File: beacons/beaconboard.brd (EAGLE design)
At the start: 101.6 x 76.2 mm, 33 parts, among them IC1 7805TV, Q1 2N3904

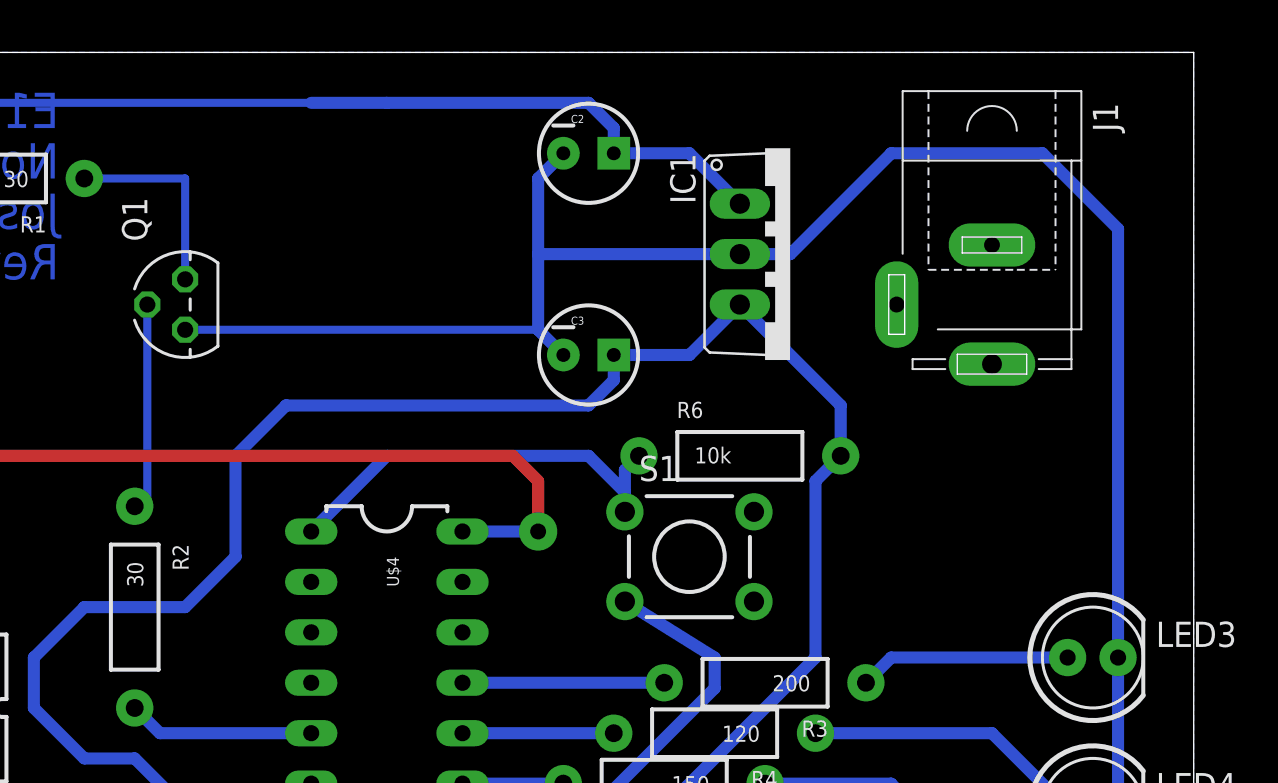
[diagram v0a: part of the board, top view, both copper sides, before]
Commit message: added DC jack; fixed NPN base resistor val
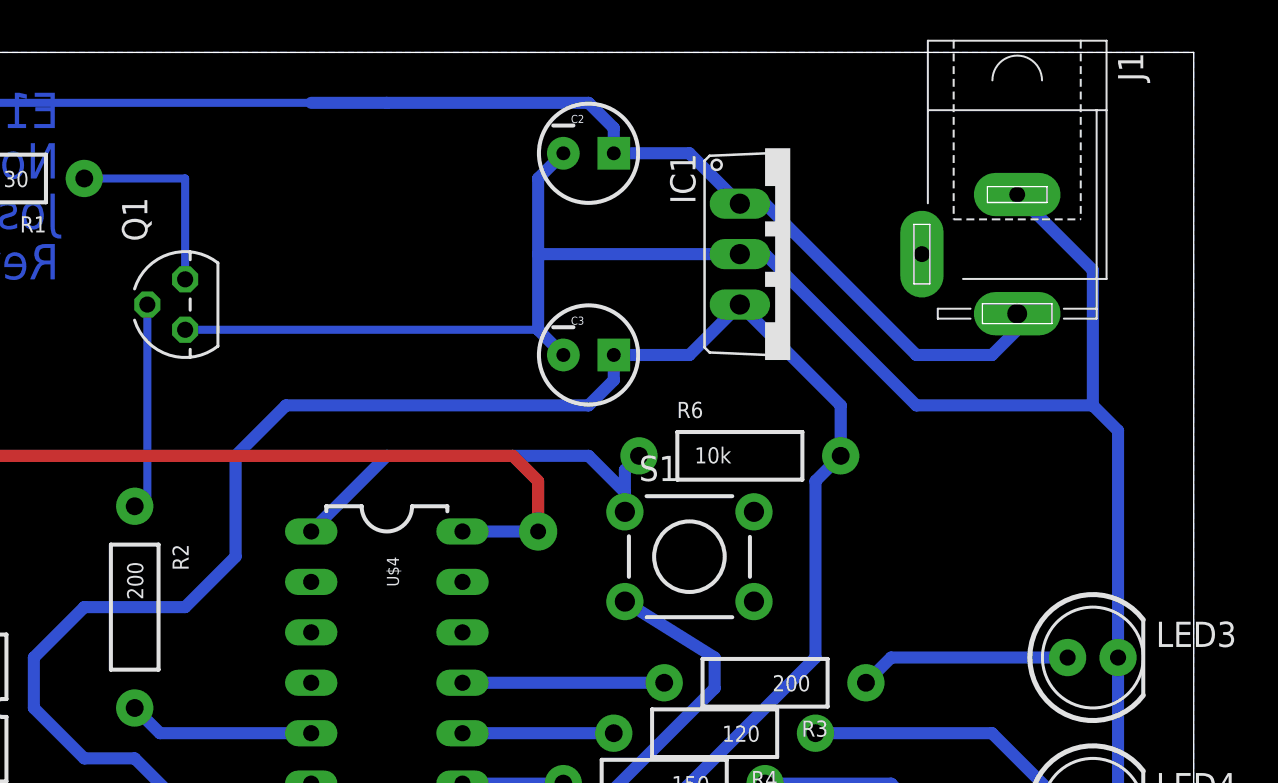
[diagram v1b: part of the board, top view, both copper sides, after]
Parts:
- R2: value 30 -> 200
- moved J1 2.84 mm to (92.7, 66.0)
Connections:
- net GND: now also J1.1
- net VDD: now also J1.3
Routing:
- net VDD: track 87.9 -> 106.4 mm
- net GND: track 409.8 -> 411.9 mm
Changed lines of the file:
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@@
 <element name="U$4" library="hmcfabstudio" package="DIL28-3" value="ATMEGA328" x="60.96" y="35.56" rot="R270"/>
 <element name="Q1" library="transistor-small-signal" package="TO92D" value="2N3904" x="50.8" y="63.5" rot="R90"/>
-<element name="J1" library="con-jack" package="SPC4078" value="" x="91.44" y="63.5" rot="R270">
-<attribute name="OC_NEWARK" value="unknown" x="91.44" y="63.5" size="1.778" layer="27" rot="R270" display="off"/>
-<attribute name="MPN" value="" x="91.44" y="63.5" size="1.778" layer="27" rot="R270" display="off"/>
-<attribute name="MF" value="" x="91.44" y="63.5" size="1.778" layer="27" rot="R270" display="off"/>
-<attribute name="OC_FARNELL" value="unknown" x="91.44" y="63.5" size="1.778" layer="27" rot="R270" display="off"/>
+<element name="J1" library="con-jack" package="SPC4078" value="" x="92.71" y="66.04" rot="R270">
+<attribute name="OC_NEWARK" value="unknown" x="92.71" y="66.04" size="1.778" layer="27" rot="R270" display="off"/>
+<attribute name="MPN" value="" x="92.71" y="66.04" size="1.778" layer="27" rot="R270" display="off"/>
+<attribute name="MF" value="" x="92.71" y="66.04" size="1.778" layer="27" rot="R270" display="off"/>
+<attribute name="OC_FARNELL" value="unknown" x="92.71" y="66.04" size="1.778" layer="27" rot="R270" display="off"/>
 </element>
 <element name="IC1" library="linear" package="TO220V" value="7805TV" x="81.28" y="66.04" rot="R270"/>
@@
 <element name="LED2" library="led" package="CP41B" value="" x="38.1" y="33.02" rot="R90"/>
 <element name="R1" library="SparkFun-Resistors" package="AXIAL-0.4" value="30" x="40.64" y="69.85" rot="R180"/>
-<element name="R2" library="SparkFun-Resistors" package="AXIAL-0.4" value="30" x="48.26" y="48.26" rot="R270"/>
+<element name="R2" library="SparkFun-Resistors" package="AXIAL-0.4" value="200" x="48.26" y="48.26" rot="R270"/>
 <element name="R3" library="SparkFun-Resistors" package="AXIAL-0.4" value="200" x="80.01" y="44.45" rot="R180"/>
 <element name="R4" library="SparkFun-Resistors" package="AXIAL-0.4" value="120" x="77.47" y="41.91" rot="R180"/>
@@
 <wire x1="27.94" y1="7.62" x2="31.75" y2="3.81" width="0.6096" layer="16"/>
 <wire x1="46.99" y1="3.81" x2="31.75" y2="3.81" width="0.6096" layer="16"/>
-<wire x1="86.36" y1="71.12" x2="81.28" y2="66.04" width="0.6096" layer="16"/>
-<wire x1="81.28" y1="66.04" x2="78.74" y2="66.04" width="0.6096" layer="16"/>
-<wire x1="86.36" y1="71.12" x2="93.98" y2="71.12" width="0.6096" layer="16"/>
-<wire x1="93.98" y1="71.12" x2="97.79" y2="67.31" width="0.6096" layer="16"/>
-<wire x1="97.79" y1="67.31" x2="97.79" y2="45.72" width="0.6096" layer="16"/>
+<wire x1="87.63" y1="58.42" x2="80.01" y2="66.04" width="0.6096" layer="16"/>
+<wire x1="80.01" y1="66.04" x2="78.74" y2="66.04" width="0.6096" layer="16"/>
+<wire x1="87.63" y1="58.42" x2="96.52" y2="58.42" width="0.6096" layer="16"/>
+<wire x1="96.52" y1="58.42" x2="97.79" y2="57.15" width="0.6096" layer="16"/>
+<wire x1="97.79" y1="57.15" x2="97.79" y2="45.72" width="0.6096" layer="16"/>
 <wire x1="40.64" y1="25.4" x2="40.64" y2="27.94" width="0.6096" layer="16"/>
 <wire x1="40.64" y1="27.94" x2="48.26" y2="35.56" width="0.6096" layer="16"/>
@@
 <wire x1="50.8" y1="62.23" x2="68.58" y2="62.23" width="0.4064" layer="16"/>
 <wire x1="27.94" y1="10.16" x2="27.94" y2="25.4" width="0.4064" layer="16"/>
-<wire x1="5.08" y1="36.83" x2="5.08" y2="38.1" width="0" layer="19" extent="16-16"/>
+<contactref element="J1" pad="1"/>
+<wire x1="96.52" y1="58.42" x2="96.52" y2="65.23" width="0.6096" layer="16"/>
+<wire x1="96.52" y1="65.23" x2="92.71" y2="69.04" width="0.6096" layer="16"/>
 </signal>
 <signal name="VDD">
@@
 <wire x1="40.64" y1="45.72" x2="40.64" y2="73.66" width="0.4064" layer="16"/>
 <wire x1="40.64" y1="73.66" x2="60.96" y2="73.66" width="0.4064" layer="16"/>
+<contactref element="J1" pad="3"/>
+<wire x1="92.71" y1="63.04" x2="92.71" y2="62.23" width="0.6096" layer="16"/>
+<wire x1="92.71" y1="62.23" x2="91.44" y2="60.96" width="0.6096" layer="16"/>
+<wire x1="91.44" y1="60.96" x2="87.63" y2="60.96" width="0.6096" layer="16"/>
+<wire x1="87.63" y1="60.96" x2="80.01" y2="68.58" width="0.6096" layer="16"/>
+<wire x1="80.01" y1="68.58" x2="78.74" y2="68.58" width="0.6096" layer="16"/>
 <wire x1="40.64" y1="35.56" x2="40.64" y2="40.64" width="0" layer="19" extent="1-1"/>
 <wire x1="40.64" y1="45.72" x2="40.64" y2="40.64" width="0" layer="19" extent="1-1"/>
